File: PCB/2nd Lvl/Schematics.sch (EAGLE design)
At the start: 37 parts, among them U1 MSP430FR5969, U2 TPS73533_DRV_6, U3 BQ27510-G2_DRZ_12, U4 SPARKFUN_USD-SOCKETSMD

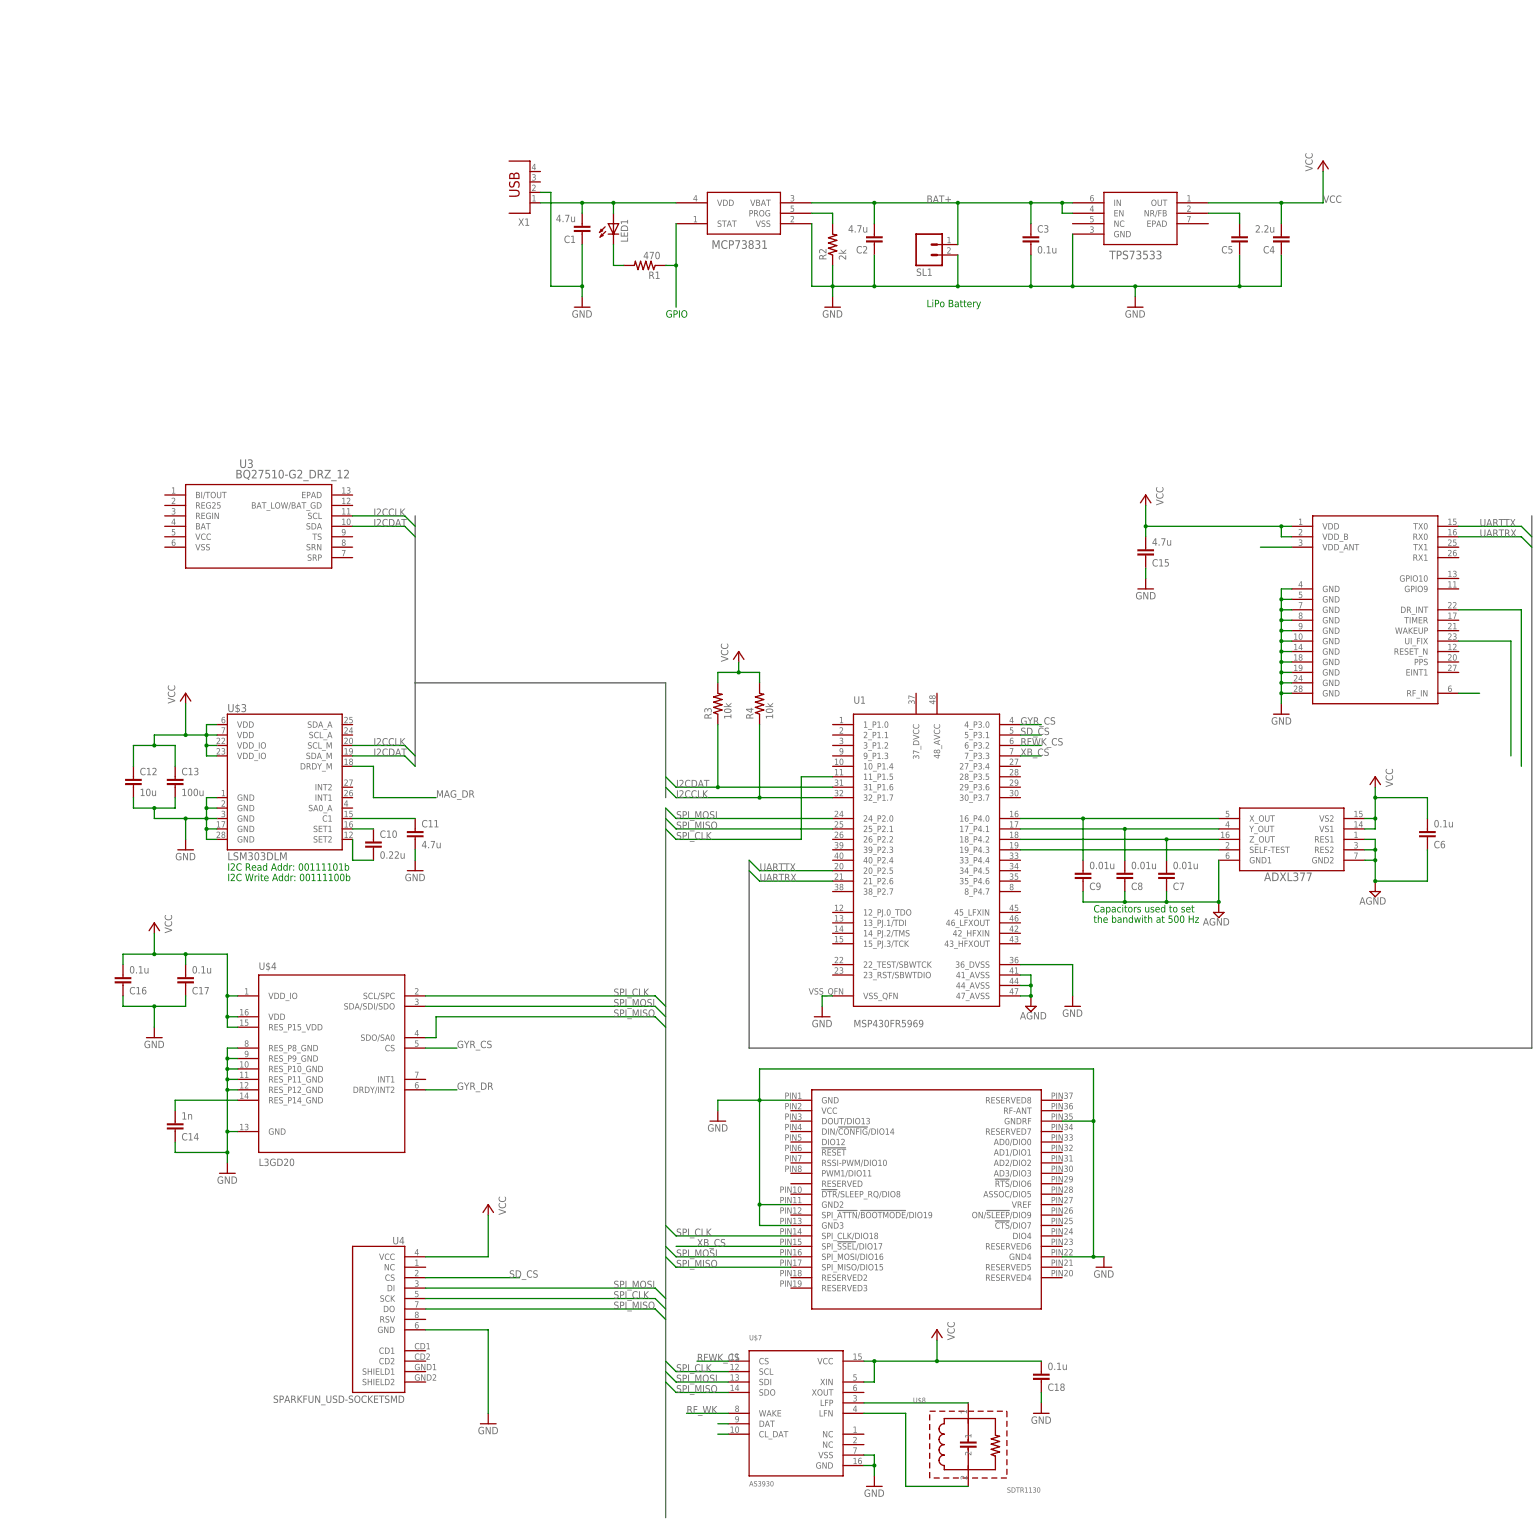
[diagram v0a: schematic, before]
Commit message: Added PCB files, GDrive and Dropbox weren't playing nicely
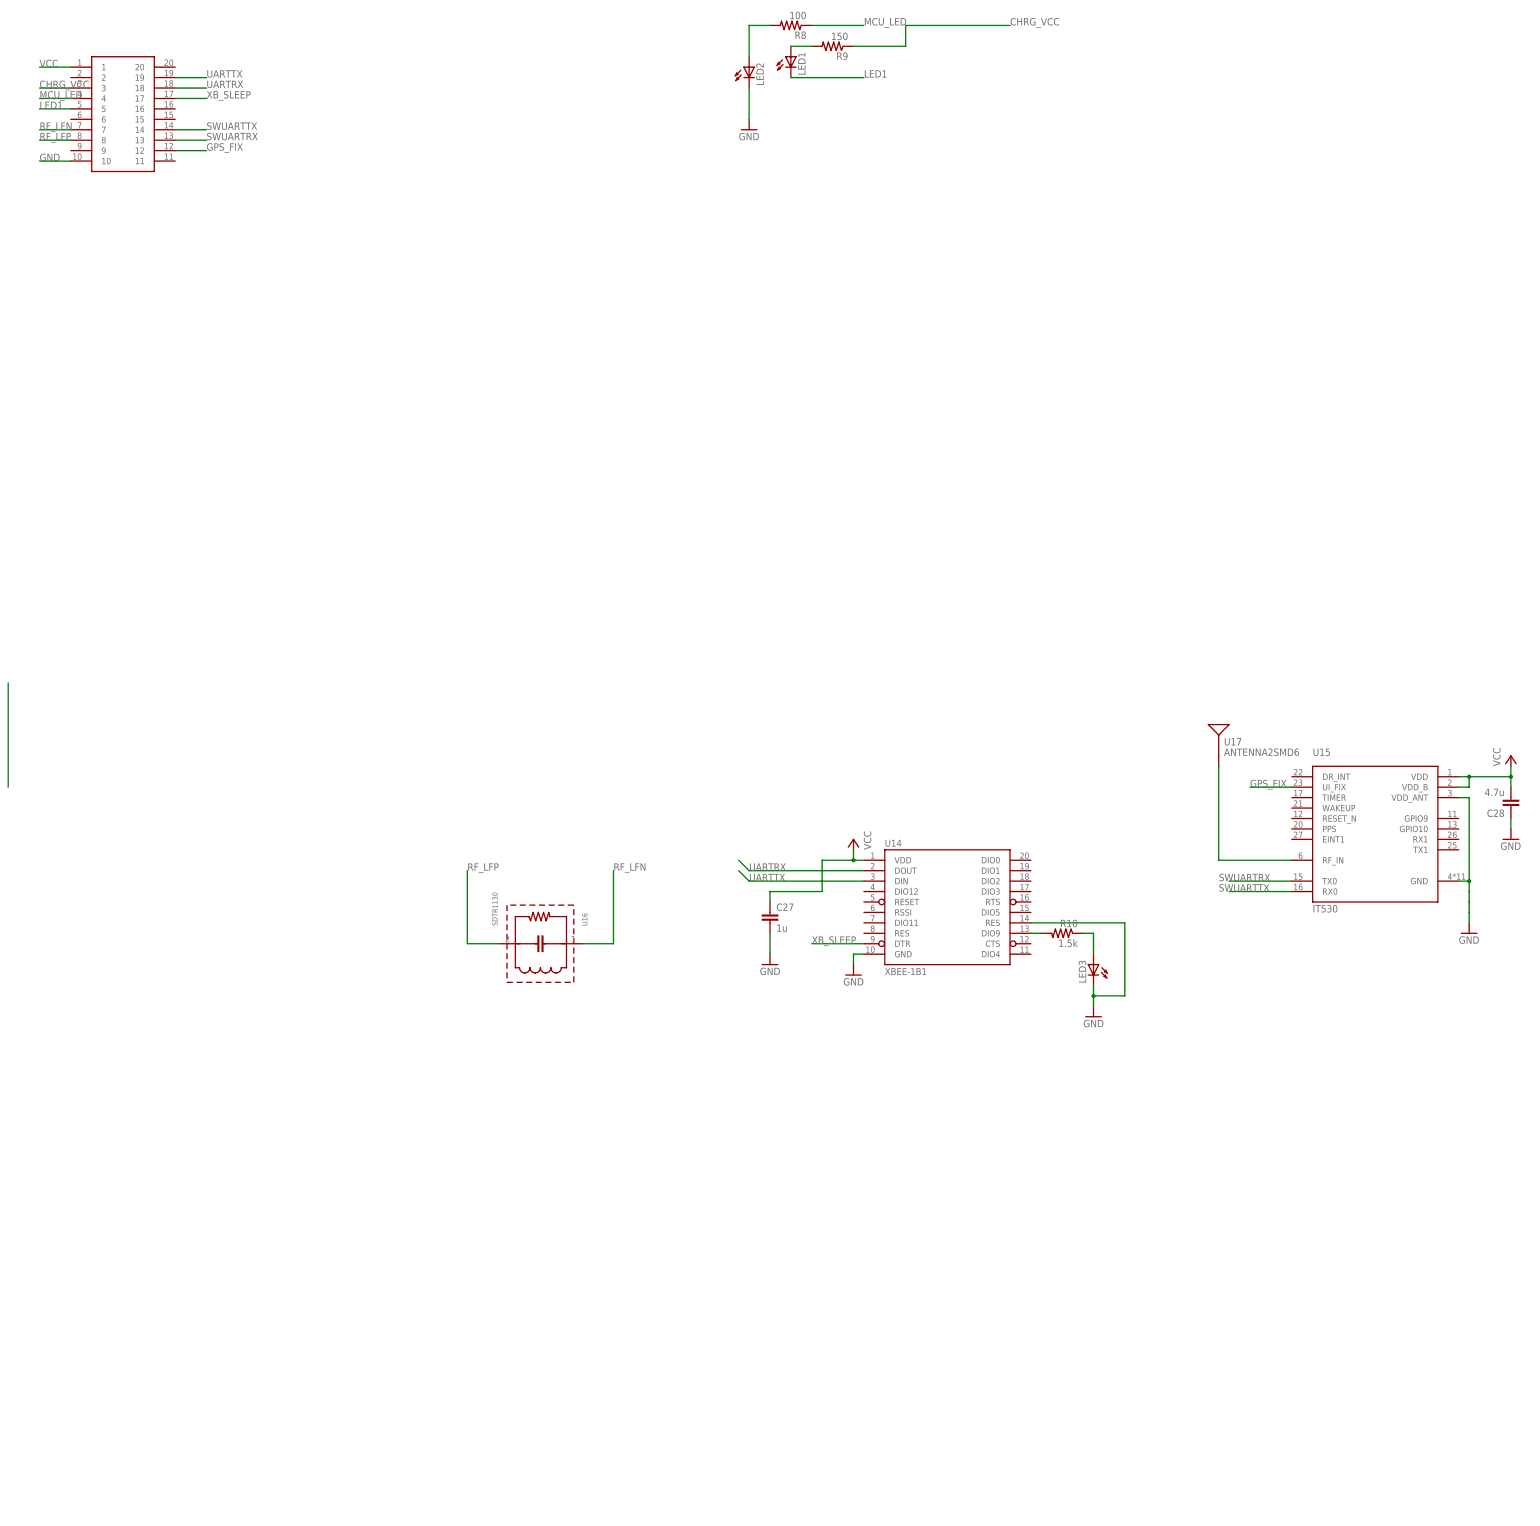
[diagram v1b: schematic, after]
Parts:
- removed C1, C15, C2: 4.7u, rcl:C-EU025-025X050
- removed C10: 0.22u, rcl:C-EU025-024X044
- removed C11: 4.7u, rcl:C-EU025-024X044
- removed C12: 10u, rcl:C-EU025-024X044
- removed C13: 100u, rcl:C-EU025-024X044
- removed C14: 1n, rcl:C-EU025-025X050
- removed C16, C17, C18, C6: 0.1u, rcl:C-EU025-025X050
- removed C3: 0.1u, rcl:C-EU025-024X044
- removed C4: 2.2u, rcl:C-EU025-025X050
- removed C5: (no value), rcl:C-EU025-025X050
- removed C7, C8, C9: 0.01u, rcl:C-EU025-025X050
- removed R1: 470, rcl:R-US_0204/2V
- removed R2: 2k, rcl:R-US_0204/2V
- removed R3, R4: 10k, rcl:R-US_0204/2V
- removed SL1: (no value), con-amp-quick:M02
- removed U$1: MCP73831-XXXX/OT, MCP73831:MCP73831-XXXX/OT
- removed U$2: ADXL377, Micro2:ADXL377
- removed U$3: LSM303DLM, Micro2:LSM303DLM
- removed U$4: L3GD20, Micro2:L3GD20
- removed U$5: QUBIQ_XBEE-SMT, Micro2:QUBIQ_XBEE-SMT
- removed U$6: IT530, Micro2:IT530
- removed U$7: AS3930, Micro2:AS3930
- removed U$8: SDTR1130, Micro2:SDTR1130
- removed U1: MSP430FR5969, hijack:MSP430FR5969
- removed U2: TPS73533_DRV_6, TPS73533:TPS73533_DRV_6
- removed U3: BQ27510-G2_DRZ_12, Micro2:BQ27510-G2_DRZ_12
- removed U4: SPARKFUN_USD-SOCKETSMD, Micro2:SPARKFUN_USD-SOCKETSMD
- removed X1: (no value), con-berg:PN61729
- added C27: 1u, rcl:C-EUC0603
- added C28: 4.7u, rcl:C-EUC0603
- added JP4: 20-HEAD, Micro2:20-HEAD
- added LED2, LED3: (no value), led:LED
- added R10: 1.5k, rcl:R-US_R0603
- added R8: 100, rcl:R-US_R0603
- added R9: 150, rcl:R-US_R0603
- added U14: XBEE-1B1, SparkFun-RF:XBEE-1B1
- added U15: IT530, Micro2:IT530
- added U16: SDTR1130, Micro2:SDTR1130
- added U17: ANTENNA2SMD6, SparkFun-RF:ANTENNA2SMD6
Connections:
- removed net AGND: C6.1, C7.1, C8.1, C9.1, U$2.GND1, U$2.GND2, U$2.RES1, U$2.RES2, U1.41_AVSS, U1.44_AVSS, U1.47_AVSS
- removed net BAT+: C2.2, C3.1, SL1.1, U$1.VBAT, U2.EN, U2.IN
- removed net GYR_CS: U$4.CS, U1.4_P3.0
- removed net GYR_DR: U$4.DRDY/INT2
- removed net I2CCLK: R4.1, U$3.SCL_M, U1.32_P1.7, U3.SCL
- removed net I2CDAT: R3.1, U$3.SDA_M, U1.31_P1.6, U3.SDA
- removed net MAG_DR: U$3.DRDY_M
- removed net N$1: C1.2, LED1.A, U$1.VDD, X1.1
- removed net N$10: C10.2, U$3.SET2
- removed net N$11: C11.1, U$3.C1
- removed net N$12: U$7.LFN, U$8.2
- removed net N$13: U$7.CL_DAT
- removed net N$15: U$7.LFP, U$8.1
- removed net N$16: U$6.VDD_ANT
- removed net N$17: U$6.DR_INT
- removed net N$18: C9.2, U$2.X_OUT, U1.16_P4.0
- removed net N$19: U$6.UI_FIX
- removed net N$2: LED1.C, R1.2
- removed net N$20: C8.2, U$2.Y_OUT, U1.17_P4.1
- removed net N$21: C7.2, U$2.Z_OUT, U1.18_P4.2
- removed net N$5: U$2.SELF-TEST, U1.19_P4.3
- removed net N$6: U$7.DAT
- removed net N$7: C5.2, U2.NR/FB
- removed net N$8: C14.2, U$4.RES_P14_GND
- removed net N$9: C10.1, U$3.SET1
- removed net RFWK_CS: U$7.CS, U1.6_P3.2
- removed net RF_WK: U$7.WAKE
- removed net SD_CS: U1.5_P3.1, U4.CS
- removed net SPI_CLK: U$4.SCL/SPC, U$5.SPI_CLK/DIO18, U$7.SCL, U1.11_P1.5, U4.SCK
- removed net SPI_MISO: U$4.SDO/SA0, U$5.SPI_MISO/DIO15, U$7.SDO, U1.25_P2.1, U4.DO
- removed net SPI_MOSI: U$4.SDA/SDI/SDO, U$5.SPI_MOSI/DIO16, U$7.SDI, U1.24_P2.0, U4.DI
- removed net XB_CS: U$5.SPI_!SSEL!/DIO17, U1.7_P3.3
- new net CHRG_VCC: JP4.3, R9.1
- new net GPS_FIX: JP4.12, U15.UI_FIX
- new net LED1: JP4.5, LED1.C
- new net MCU_LED: JP4.4, R8.1
- new net N$36: LED1.A, R9.2
- new net N$41: LED2.A, R8.2
- new net RF_LFN: JP4.7, U16.1
- new net RF_LFP: JP4.8, U16.2
- new net SWUARTRX: JP4.13, U15.TX0
- new net SWUARTTX: JP4.14, U15.RX0
- new net XB_SLEEP: JP4.17, U14.DTR
- net GND: now also C27.2, C28.1, JP4.10, LED2.C, LED3.C, U14.GND, U14.RES@14, U15.GND, U15.VDD_ANT; no longer C1.1, C11.2, C12.2, C13.2, C14.1, C15.1, C16.1, C17.1, C18.1, C2.1, C3.2, C4.1, C5.1, R2.1, SL1.2, U$1.VSS, U$3.GND@1, U$3.GND@17, U$3.GND@2, U$3.GND@28, U$3.GND@3, U$4.GND, U$4.RES_P10_GND, U$4.RES_P11_GND, U$4.RES_P12_GND, U$4.RES_P8_GND, U$4.RES_P9_GND, U$5.GND, U$5.GND2, U$5.GND3, U$5.GND4, U$5.GNDRF, U$6.GND@10, U$6.GND@14, U$6.GND@18, U$6.GND@19, U$6.GND@24, U$6.GND@28, U$6.GND@4, U$6.GND@5, U$6.GND@7, U$6.GND@8, U$6.GND@9, U$7.GND@16, U$7.VSS, U1.36_DVSS, U1.VSS_QFN, U2.GND, U4.GND, X1.2
- net N$14: now also U15.RF_IN, U17.SIGNAL; no longer U$6.RF_IN
- net N$3: now also LED3.A, R10.1; no longer R1.1, U$1.STAT
- net N$4: now also R10.2, U14.DIO9; no longer R2.2, U$1.PROG
- net UARTRX: now also JP4.18, U14.DOUT; no longer U$6.RX0, U1.21_P2.6
- net UARTTX: now also JP4.19, U14.DIN; no longer U$6.TX0, U1.20_P2.5
- net VCC: now also C27.1, C28.2, JP4.1, U14.VDD, U15.VDD, U15.VDD_B; no longer C12.1, C13.1, C15.2, C16.2, C17.2, C18.2, C4.2, C6.2, R3.2, R4.2, U$2.VS1, U$2.VS2, U$3.VDD, U$3.VDD@7, U$3.VDD_IO@22, U$3.VDD_IO@23, U$4.RES_P15_VDD, U$4.VDD, U$4.VDD_IO, U$6.VDD, U$6.VDD_B, U$7.VCC, U$7.XIN, U2.OUT, U4.VCC
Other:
- note removed: "Capacitors used to set"
- note removed: "GPIO"
- note removed: "I2C Read Addr: 00111101b"
- note removed: "I2C Write Addr: 00111100b"
- note removed: "LiPo Battery"
- note removed: "the bandwith at 500 Hz"
- moved on the sheet: LED1

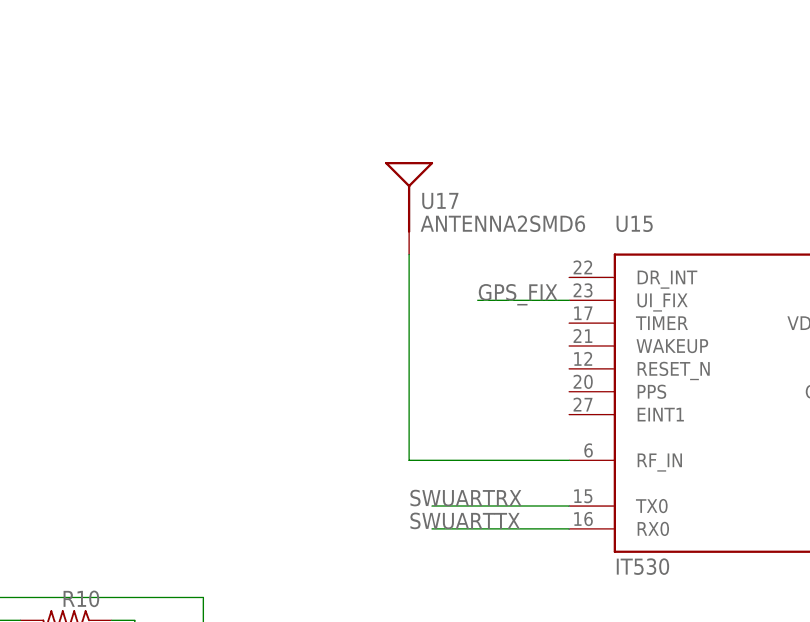
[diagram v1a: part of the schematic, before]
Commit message: Added GPS_FIX Led to 2nd lvl
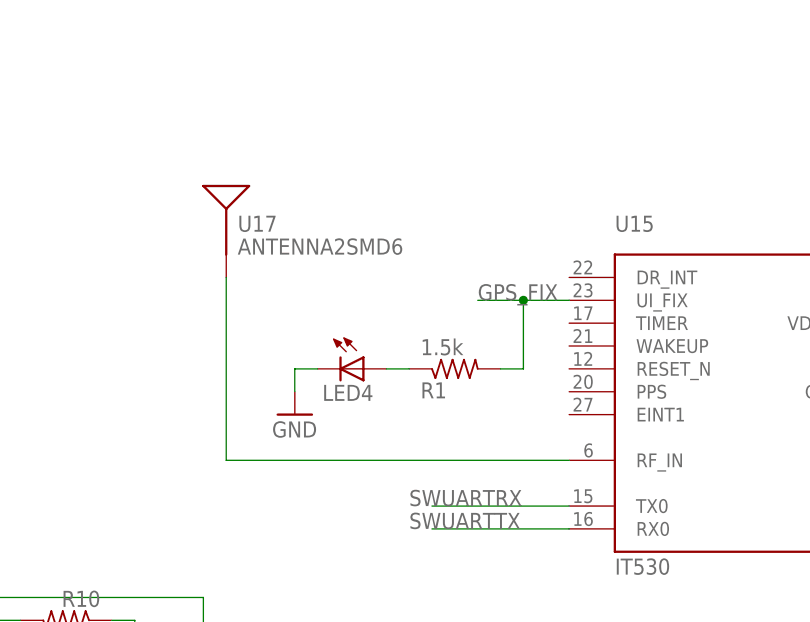
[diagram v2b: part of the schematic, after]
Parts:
- added LED4: (no value), led:LED
- added R1: 1.5k, rcl:R-US_R0603
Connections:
- new net N$1: LED4.A, R1.1
- net GND: now also LED4.C
- net GPS_FIX: now also R1.2
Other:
- moved on the sheet: U17
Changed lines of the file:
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@@
 <?xml version="1.0" encoding="utf-8"?>
 <!DOCTYPE eagle SYSTEM "eagle.dtd">
-<eagle version="6.0">
+<eagle version="6.2">
 <drawing>
 <settings>
@@
 <part name="JP4" library="Micro2" deviceset="20-HEAD" device=""/>
 <part name="GND1" library="supply1" deviceset="GND" device=""/>
+<part name="LED4" library="led" deviceset="LED" device=""/>
+<part name="GND3" library="supply1" deviceset="GND" device=""/>
+<part name="R1" library="rcl" deviceset="R-US_" device="R0603" value="1.5k"/>
 </parts>
 <sheets>
@@
 <instance part="GND2" gate="1" x="71.12" y="-124.46" rot="MR0"/>
 <instance part="FRAME1" gate="G$1" x="-200.66" y="-134.62"/>
-<instance part="U17" gate="G$1" x="101.6" y="-58.42"/>
+<instance part="U17" gate="G$1" x="81.28" y="-60.96"/>
 <instance part="U14" gate="G$1" x="35.56" y="-96.52"/>
 <instance part="GND14" gate="1" x="12.7" y="-114.3" rot="MR0"/>
@@
 <instance part="JP4" gate="G$1" x="-165.1" y="93.98"/>
 <instance part="GND1" gate="1" x="-12.7" y="91.44"/>
+<instance part="LED4" gate="G$1" x="96.52" y="-76.2" rot="R270"/>
+<instance part="GND3" gate="1" x="88.9" y="-81.28"/>
+<instance part="R1" gate="G$1" x="106.68" y="-76.2" rot="MR180"/>
 </instances>
 <busses>
@@
 <wire x1="-12.7" y1="101.6" x2="-12.7" y2="93.98" width="0.1524" layer="91"/>
 <pinref part="GND1" gate="1" pin="GND"/>
+</segment>
+<segment>
+<pinref part="LED4" gate="G$1" pin="C"/>
+<wire x1="91.44" y1="-76.2" x2="88.9" y2="-76.2" width="0.1524" layer="91"/>
+<pinref part="GND3" gate="1" pin="GND"/>
+<wire x1="88.9" y1="-76.2" x2="88.9" y2="-78.74" width="0.1524" layer="91"/>
 </segment>
 </net>
@@
 <net name="N$14" class="0">
 <segment>
-<wire x1="101.6" y1="-63.5" x2="101.6" y2="-86.36" width="0.1524" layer="91"/>
-<wire x1="101.6" y1="-86.36" x2="119.38" y2="-86.36" width="0.1524" layer="91"/>
+<wire x1="81.28" y1="-66.04" x2="81.28" y2="-86.36" width="0.1524" layer="91"/>
+<wire x1="81.28" y1="-86.36" x2="119.38" y2="-86.36" width="0.1524" layer="91"/>
 <pinref part="U15" gate="G$1" pin="RF_IN"/>
 <pinref part="U17" gate="G$1" pin="SIGNAL"/>
@@
 <segment>
 <pinref part="U15" gate="G$1" pin="UI_FIX"/>
-<wire x1="119.38" y1="-68.58" x2="109.22" y2="-68.58" width="0.1524" layer="91"/>
 <label x="109.22" y="-68.58" size="1.778" layer="95"/>
+<wire x1="119.38" y1="-68.58" x2="114.3" y2="-68.58" width="0.1524" layer="91"/>
+<pinref part="R1" gate="G$1" pin="2"/>
+<wire x1="114.3" y1="-68.58" x2="109.22" y2="-68.58" width="0.1524" layer="91"/>
+<wire x1="111.76" y1="-76.2" x2="114.3" y2="-76.2" width="0.1524" layer="91"/>
+<wire x1="114.3" y1="-76.2" x2="114.3" y2="-68.58" width="0.1524" layer="91"/>
+<junction x="114.3" y="-68.58"/>
 </segment>
 <segment>
@@
 </segment>
 </net>
+<net name="N$1" class="0">
+<segment>
+<pinref part="R1" gate="G$1" pin="1"/>
+<pinref part="LED4" gate="G$1" pin="A"/>
+<wire x1="101.6" y1="-76.2" x2="99.06" y2="-76.2" width="0.1524" layer="91"/>
+</segment>
+</net>

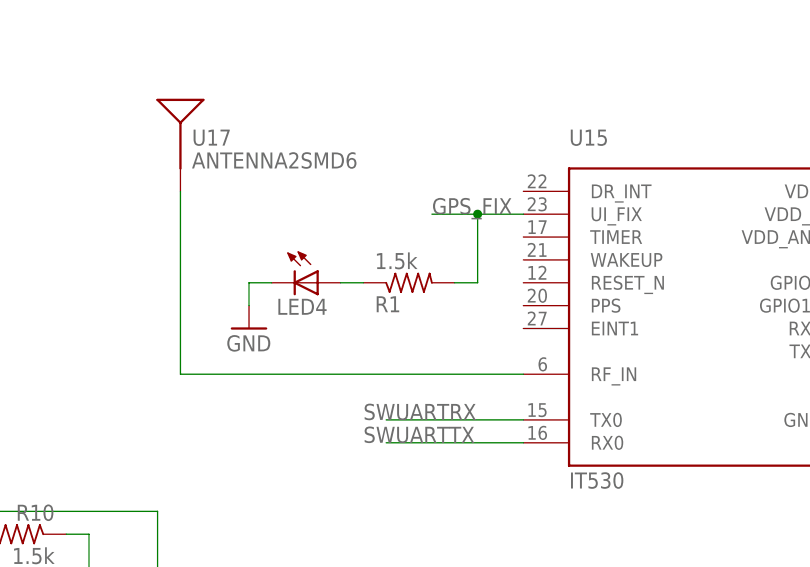
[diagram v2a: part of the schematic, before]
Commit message: Updated schematic values
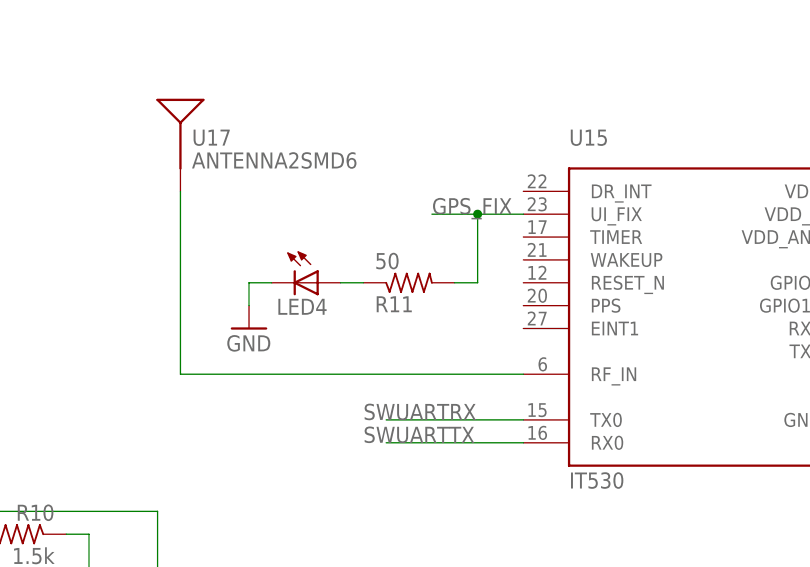
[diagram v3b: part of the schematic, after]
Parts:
- R11: value 1.5k -> 50
- renumbered R1 to R11
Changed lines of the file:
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@@
 <?xml version="1.0" encoding="utf-8"?>
 <!DOCTYPE eagle SYSTEM "eagle.dtd">
-<eagle version="6.2">
+<eagle version="6.0">
 <drawing>
 <settings>
@@
 <part name="LED4" library="led" deviceset="LED" device=""/>
 <part name="GND3" library="supply1" deviceset="GND" device=""/>
-<part name="R1" library="rcl" deviceset="R-US_" device="R0603" value="1.5k"/>
+<part name="R11" library="rcl" deviceset="R-US_" device="R0603" value="50"/>
 </parts>
 <sheets>
@@
 <instance part="LED4" gate="G$1" x="96.52" y="-76.2" rot="R270"/>
 <instance part="GND3" gate="1" x="88.9" y="-81.28"/>
-<instance part="R1" gate="G$1" x="106.68" y="-76.2" rot="MR180"/>
+<instance part="R11" gate="G$1" x="106.68" y="-76.2" rot="MR180"/>
 </instances>
 <busses>
@@
 <label x="109.22" y="-68.58" size="1.778" layer="95"/>
 <wire x1="119.38" y1="-68.58" x2="114.3" y2="-68.58" width="0.1524" layer="91"/>
-<pinref part="R1" gate="G$1" pin="2"/>
+<pinref part="R11" gate="G$1" pin="2"/>
 <wire x1="114.3" y1="-68.58" x2="109.22" y2="-68.58" width="0.1524" layer="91"/>
 <wire x1="111.76" y1="-76.2" x2="114.3" y2="-76.2" width="0.1524" layer="91"/>
@@
 <net name="N$1" class="0">
 <segment>
-<pinref part="R1" gate="G$1" pin="1"/>
+<pinref part="R11" gate="G$1" pin="1"/>
 <pinref part="LED4" gate="G$1" pin="A"/>
 <wire x1="101.6" y1="-76.2" x2="99.06" y2="-76.2" width="0.1524" layer="91"/>
